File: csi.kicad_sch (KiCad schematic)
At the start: 38 parts, among them J6 WE_68715014522, J7 WE_68715014022, T8 BSS138APW, U4 PCA9547BS,118

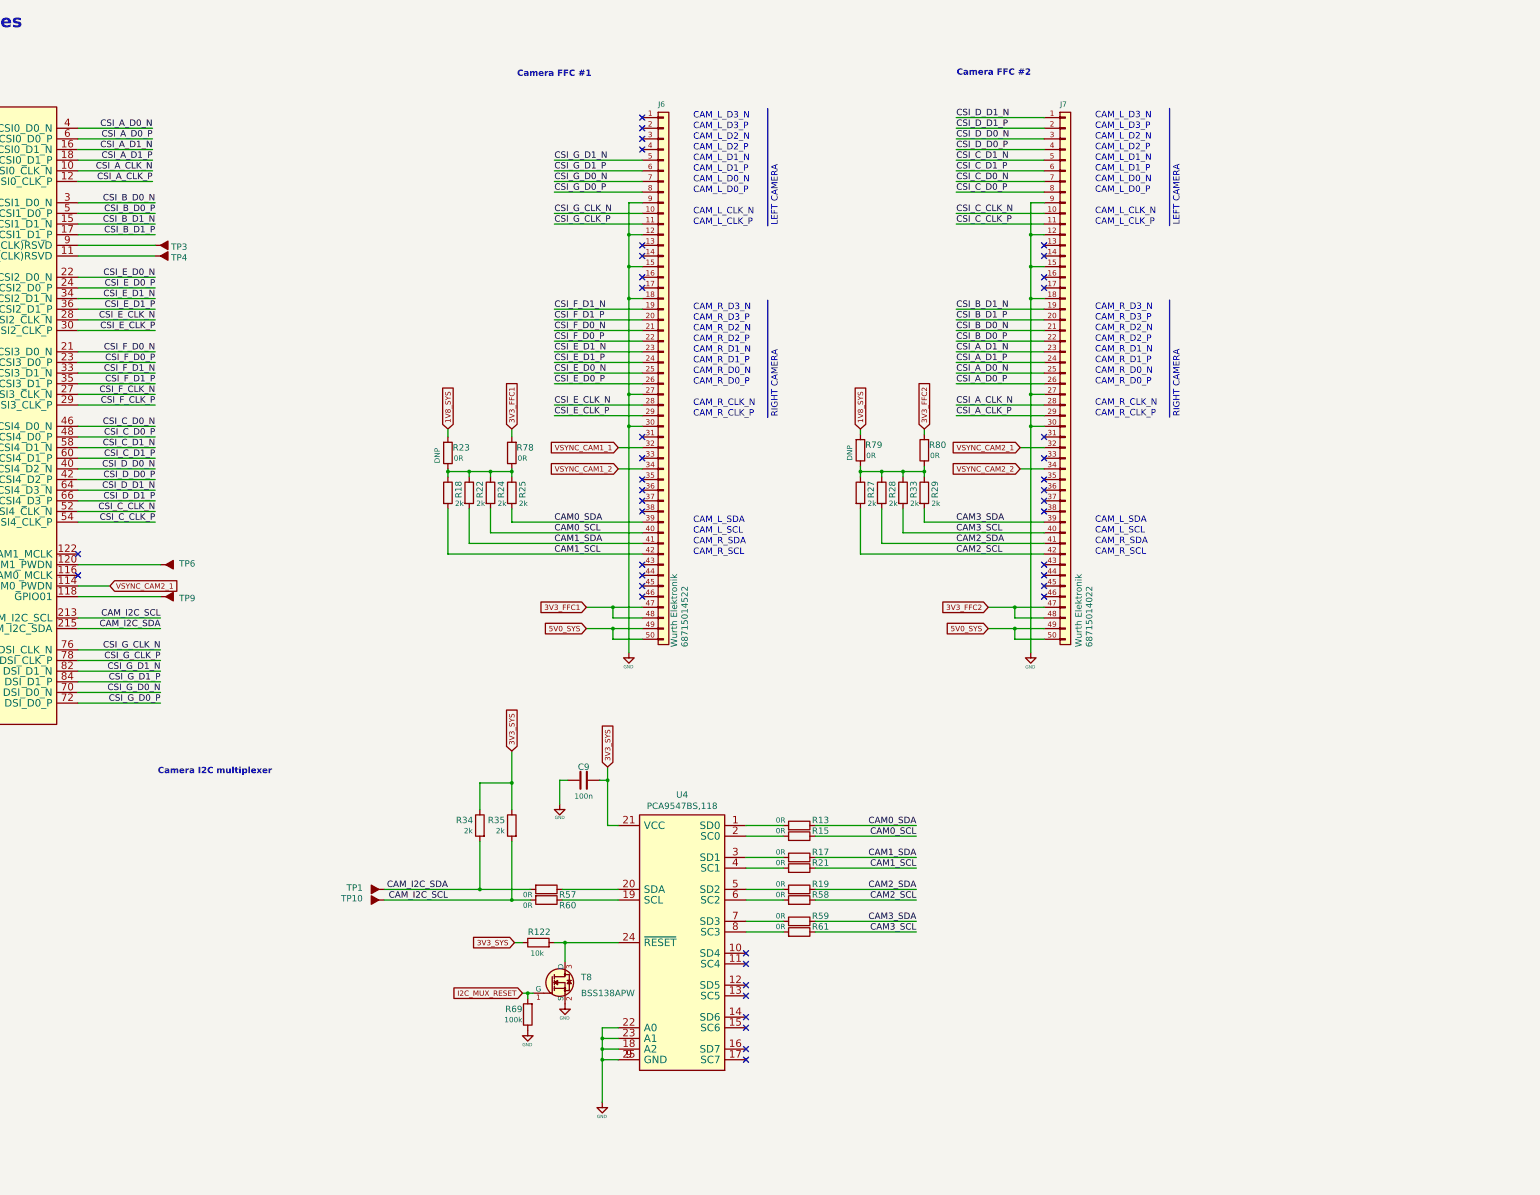
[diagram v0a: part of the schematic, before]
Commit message: WIP: Re-design base board
1. change to more common connector from JLC
2. add WIFI M.2 Key-E connector
3. add USB Hub which contained in nVidia version board
4. change DC connecotor to XT30
5. change USB Mico-B to USB Type C
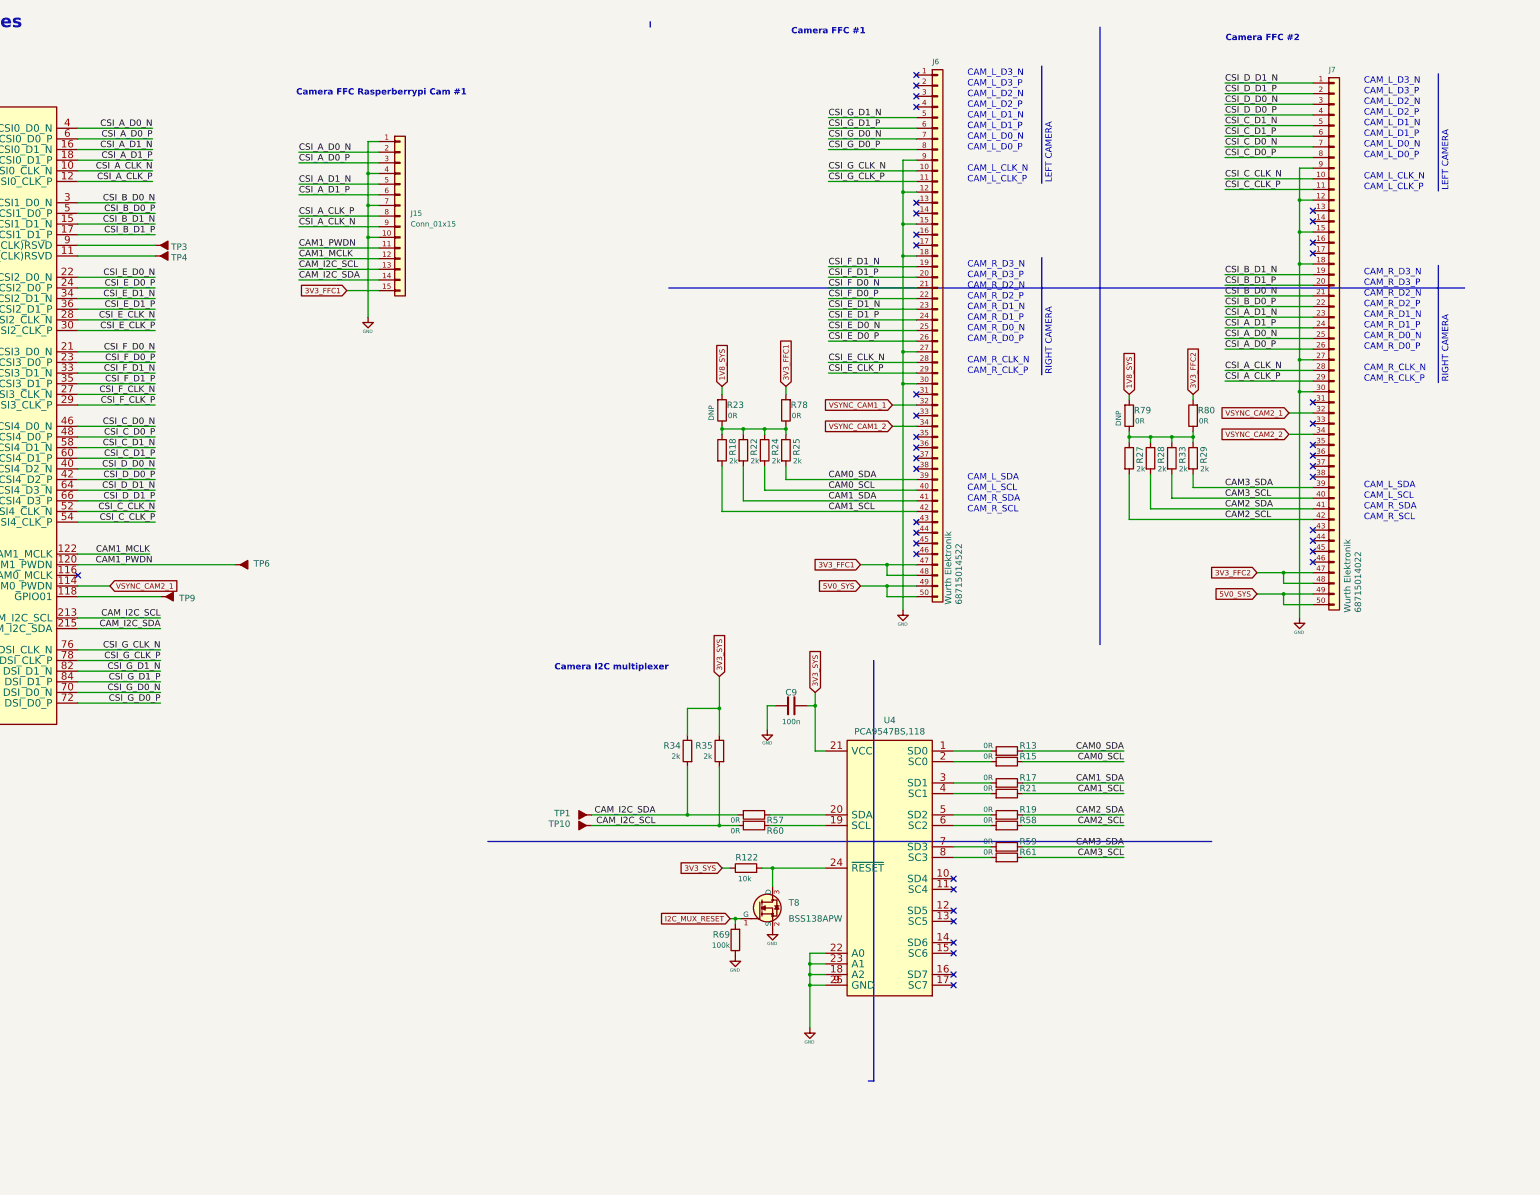
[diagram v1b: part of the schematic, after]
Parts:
- added J15: Conn_01x15, JLC_Footprint:FPC-SMD_AFA07-S15FCC-00, symbol Connector_Generic:Conn_01x15
- C9, J6, J7, R122, R13, R17, R18, R19, R21, R22, R23, R24, R25, R27, R28, R29, R33, R34, R35, R57, R58, R59, R60, R61, R69, R78, R79, R80, T8, U4: now left out of the parts list
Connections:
- net 3V3_FFC1: now also J15.15 (Pin_15)
- net CAM_I2C_SCL: now also J15.13 (Pin_13)
- net CAM_I2C_SDA: now also J15.14 (Pin_14)
- net CSI_A_CLK_N: now also J15.9 (Pin_9)
- net CSI_A_CLK_P: now also J15.8 (Pin_8)
- net CSI_A_D0_N: now also J15.2 (Pin_2)
- net CSI_A_D0_P: now also J15.3 (Pin_3)
- net CSI_A_D1_N: now also J15.5 (Pin_5)
- net CSI_A_D1_P: now also J15.6 (Pin_6)
- net GND: now also J15.1 (Pin_1), J15.10 (Pin_10), J15.4 (Pin_4), J15.7 (Pin_7)
- net CAM1_PWDN: now reaches M1.120 (CAM1_PWDN), TP6.1 (P)
- net CAM1_PWDN: now also J15.11 (Pin_11)
- net CAM1_MCLK: now reaches M1.122 (CAM1_MCLK)
- net CAM1_MCLK: now also J15.12 (Pin_12)
- no-connect marks 42 -> 41
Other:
- note added: "Camera FFC Rasperberrypi Cam #1"
- moved on the sheet: C9, J6, J7, R122, R13, R15, R17, R18, R19, R21, R22, R23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
